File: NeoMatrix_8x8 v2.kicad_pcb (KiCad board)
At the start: 2 copper layers, 71.1 x 71.1 mm, 154 parts

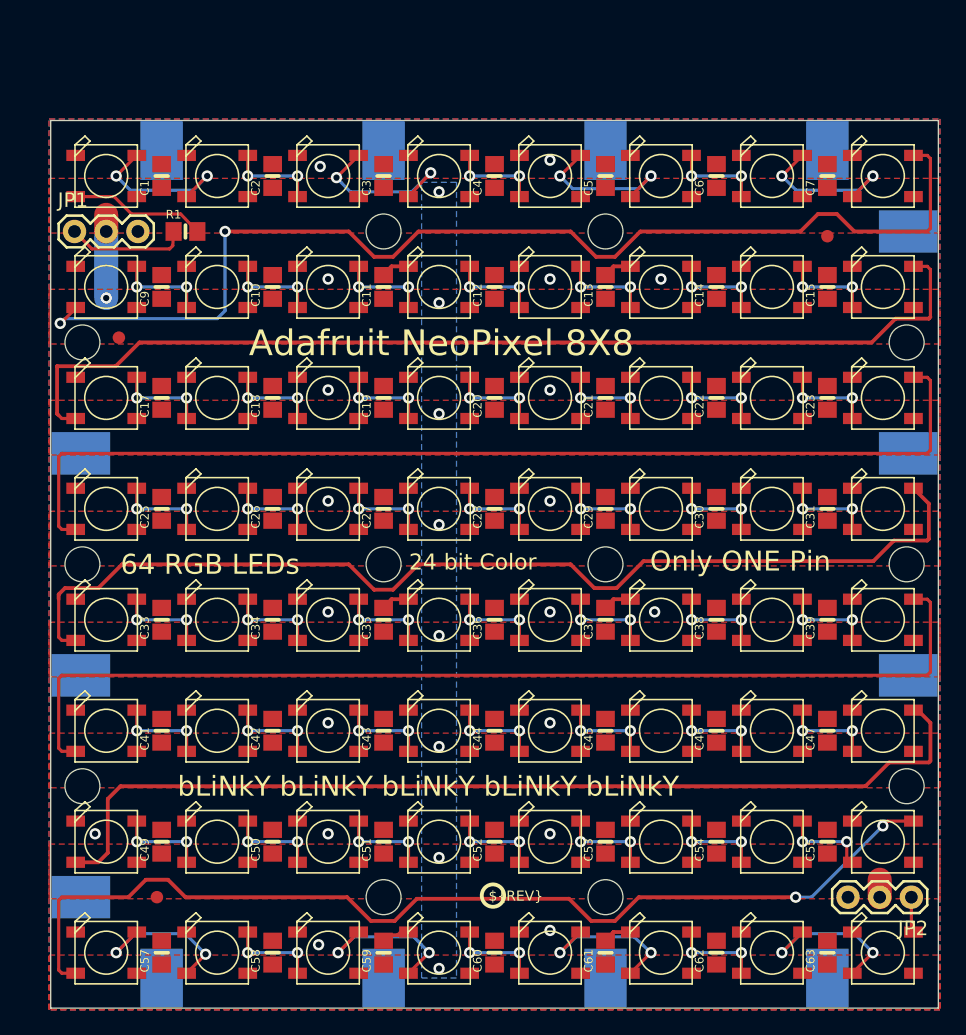
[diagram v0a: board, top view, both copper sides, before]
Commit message: Libraries corrected, references updated
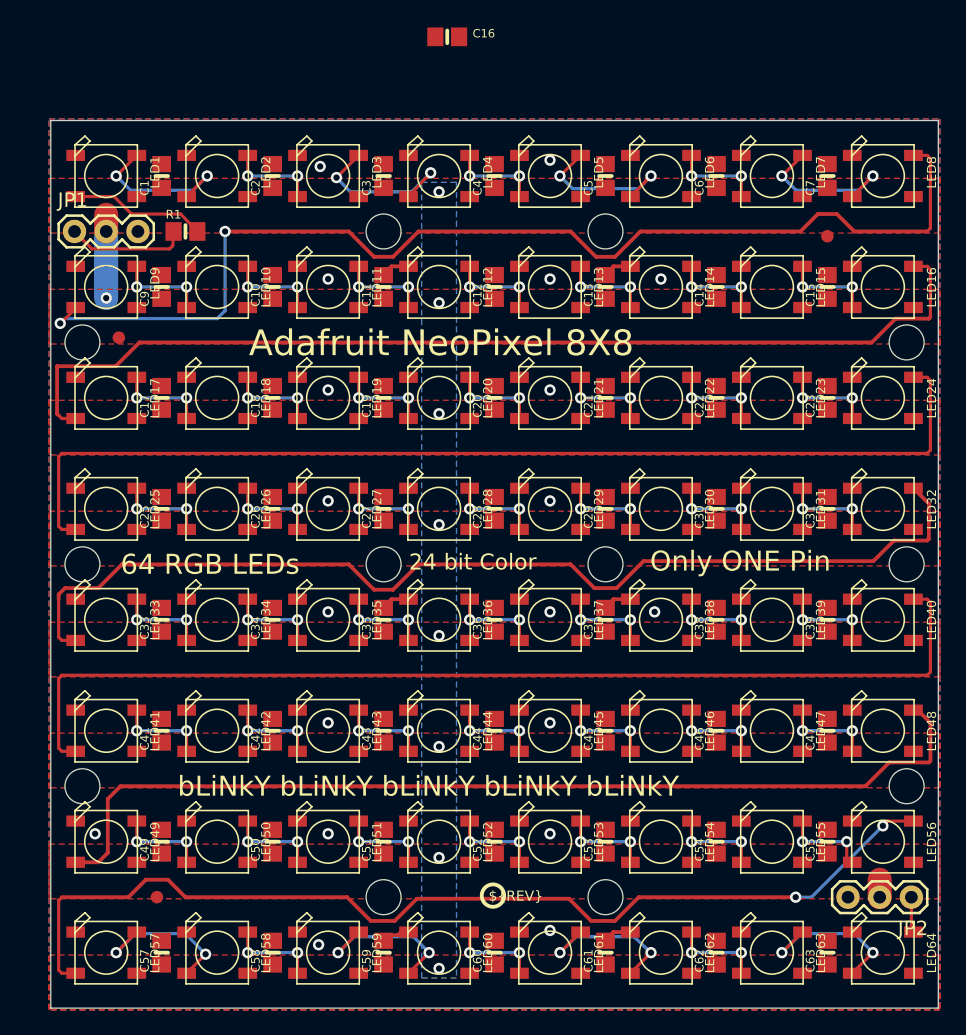
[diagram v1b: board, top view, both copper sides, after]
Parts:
- removed TP1, TP10, TP11, TP12, TP13, TP14, TP2, TP3, TP4, TP5, TP6, TP7, TP8, TP9: , Adafruit_NeoMatrix_8x8 v2:TESTPOINT_SMT
- added C16: CAP_CERAMIC0805-NOOUTLINE, Adafruit_NeoMatrix_8x8 v2:0805-NO, F.Cu at (144.7, 62.7)
- C1, C10, C11, C12, C13, C14, C15, C17, C18, C19, C2, C20, C21, C22, C23, C25, C26, C27, C28, C29, C3, C30, C31, C33, C34, C35, C36, C37, C38, C39, C4, C41, C42, C43, C44, C45, C46, C47, C49, C5, C50, C51, C52, C53, C54, C55, C57, C58, C59, C6, C60, C61, C62, C63, C7, C9: value (none) -> CAP_CERAMIC0805-NOOUTLINE
- JP1, JP2: value (none) -> M03PTH
- R1: value (none) -> RESISTOR0805_NOOUTLINE
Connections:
- net N$1 renamed /WS2812B/DIN
- net N$100 renamed /WS2812B37/DOUT
- net N$101 renamed /WS2812B38/DOUT
- net N$102 renamed /WS2812B41/DOUT
- net N$103 renamed /WS2812B42/DOUT
- net N$104 renamed /WS2812B43/DOUT
- net N$105 renamed /WS2812B44/DOUT
- net N$106 renamed /WS2812B45/DOUT
- net N$107 renamed /WS2812B46/DOUT
- net N$108 renamed /WS2812B49/DOUT
- net N$109 renamed /WS2812B50/DOUT
- net N$110 renamed /WS2812B51/DOUT
- net N$111 renamed /WS2812B52/DOUT
- net N$112 renamed /WS2812B53/DOUT
- net N$113 renamed /WS2812B54/DOUT
- net N$114 renamed /WS2812B58/DOUT
- net N$115 renamed /WS2812B59/DOUT
- net N$116 renamed /WS2812B60/DOUT
- net N$117 renamed /WS2812B61/DOUT
- net N$118 renamed /WS2812B62/DOUT
- net N$119 renamed /WS2812B32/DOUT
- net N$120 renamed /WS2812B40/DOUT
- net N$2 renamed /WS2812B7/DOUT
- net N$3 renamed /WS2812B15/DOUT
- net N$33 renamed /WS2812B16/DOUT
- net N$34 renamed /WS2812B24/DOUT
- net N$35 renamed /WS2812B25/DOUT
- net N$36 renamed /WS2812B1/DOUT
- net N$37 renamed /WS2812B2/DOUT
- net N$38 renamed /WS2812B3/DOUT
- net N$39 renamed /WS2812B4/DOUT
- net N$4 renamed /WS2812B23/DOUT
- net N$40 renamed /WS2812B5/DOUT
- net N$41 renamed /WS2812B6/DOUT
- net N$42 renamed /WS2812B10/DIN
- net N$43 renamed /WS2812B10/DOUT
- net N$44 renamed /WS2812B11/DOUT
- net N$45 renamed /WS2812B12/DOUT
- net N$46 renamed /WS2812B13/DOUT
- net N$47 renamed /WS2812B14/DOUT
- net N$48 renamed /WS2812B17/DOUT
- net N$49 renamed /WS2812B18/DOUT
- net N$5 renamed /WS2812B39/DOUT
- net N$50 renamed /WS2812B19/DOUT
- net N$51 renamed /WS2812B20/DOUT
- net N$52 renamed /WS2812B21/DOUT
- net N$53 renamed /WS2812B22/DOUT
- net N$54 renamed /WS2812B26/DOUT
- net N$55 renamed /WS2812B27/DOUT
- net N$56 renamed /WS2812B28/DOUT
- net N$57 renamed /WS2812B29/DOUT
- net N$58 renamed /WS2812B30/DOUT
- net N$59 renamed /WS2812B/DOUT
- net N$6 renamed /WS2812B31/DOUT
- net N$60 renamed /WS2812B8/DOUT
- net N$7 renamed /WS2812B47/DOUT
- net N$8 renamed /WS2812B55/DOUT
- net N$9 renamed /WS2812B63/DOUT
- net N$93 renamed /WS2812B48/DOUT
- net N$94 renamed /WS2812B56/DOUT
- net N$95 renamed /WS2812B57/DOUT
- net N$96 renamed /WS2812B33/DOUT
- net N$97 renamed /WS2812B34/DOUT
- net N$98 renamed /WS2812B35/DOUT
- net N$99 renamed /WS2812B36/DOUT

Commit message: Revised mounting holes and layout
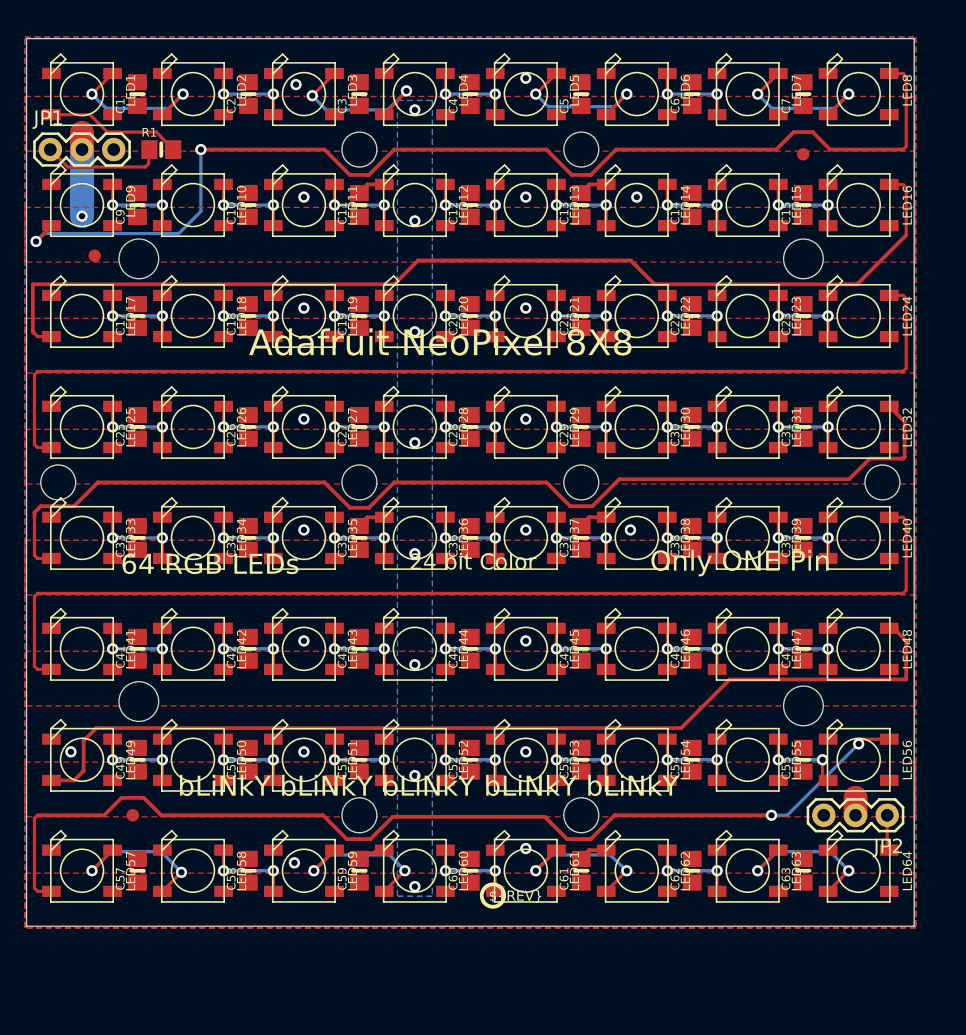
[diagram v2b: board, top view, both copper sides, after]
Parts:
- removed C16: CAP_CERAMIC0805-NOOUTLINE, Adafruit_NeoMatrix_8x8 v2:0805-NO
- moved @HOLE5 10.5 mm to (173.2, 80.8)
- moved @HOLE3 10.3 mm to (173.5, 116.3)
- moved @HOLE2 8.08 mm to (120.0, 116.1)
- moved @HOLE0 8.07 mm to (120.0, 80.5)
- moved C10 6.84 mm to (128.8, 76.2)
- moved C12 6.84 mm to (146.6, 76.2)
- moved C14 6.84 mm to (164.3, 76.2)
- moved C18 6.84 mm to (128.8, 85.1)
- moved C2 6.84 mm to (128.8, 67.3)
- moved C20 6.84 mm to (146.6, 85.1)
- moved C22 6.84 mm to (164.3, 85.1)
- moved C26 6.84 mm to (128.8, 94.0)
- moved C28 6.84 mm to (146.6, 94.0)
- moved C30 6.84 mm to (164.3, 94.0)
- moved C34 6.84 mm to (128.8, 102.9)
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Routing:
- net /WS2812B15/DOUT: track 82.3 -> 83.9 mm
- net /WS2812B47/DOUT: track 79.2 -> 78.1 mm
- net /WS2812B7/DOUT: track 90.0 -> 89.2 mm
